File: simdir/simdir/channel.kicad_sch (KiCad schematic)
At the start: 84 parts, among them J1 Conn_Coaxial, Q1 BC847, Q10 BC847, Q11 BC847, Q12 BC847, Q13 BC847, Q14 BC847, Q15 BC847, Q16 BC847, Q2 BC847, Q3 BC847, Q4 BC847, Q5 BC847, Q6 BC847, Q7 BC847, Q8 BC847, Q9 BC847, U1 MASWSS0178, U10 MASWSS0178, U11 MASWSS0178, U12 MASWSS0178, U13 MASWSS0178, U14 MASWSS0178, U15 MASWSS0178, U16 MASWSS0178, U17 LTV-847S, U18 LTV-847S, U19 74HCT595, U2 MASWSS0178, U3 MASWSS0178, U4 MASWSS0178, U5 MASWSS0178, U6 MASWSS0178, U7 MASWSS0178, U8 MASWSS0178, U9 MASWSS0178

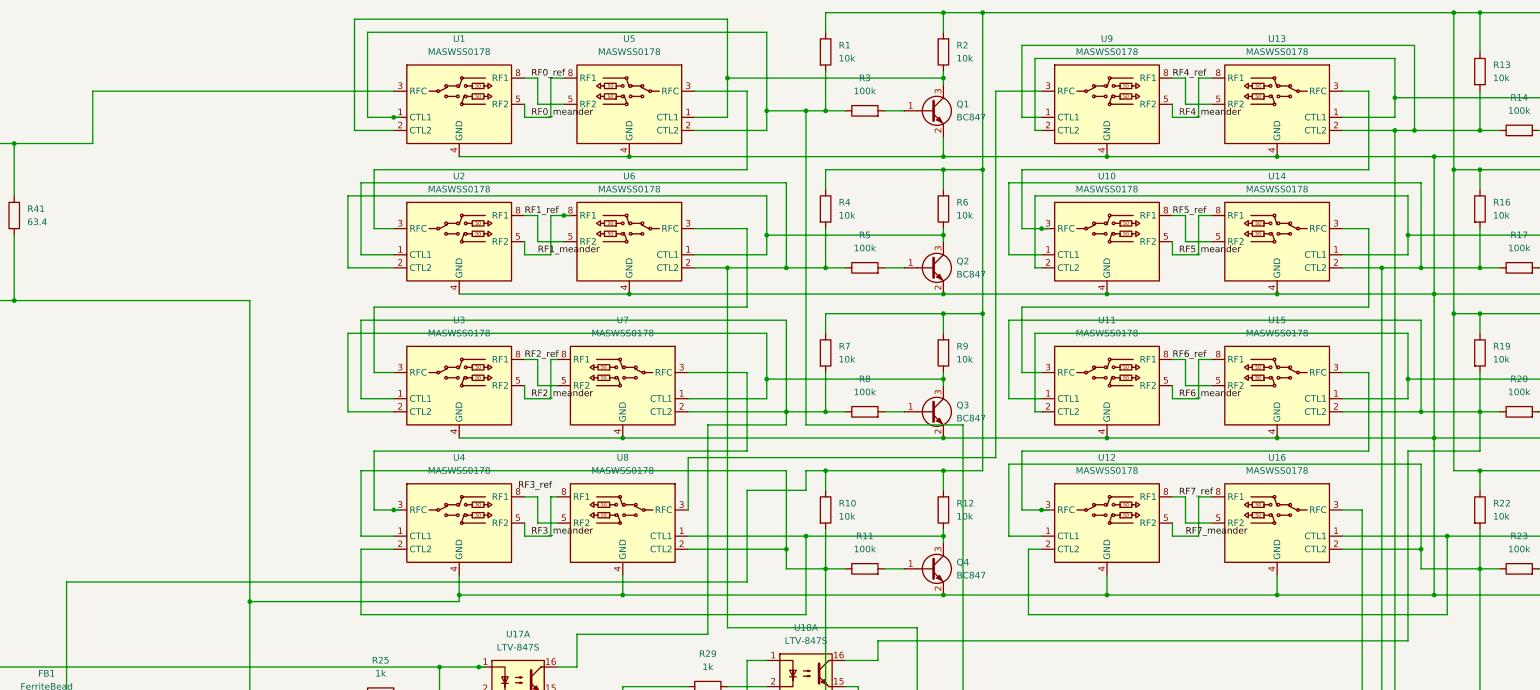
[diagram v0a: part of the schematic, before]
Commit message: Changed to new RF IC.
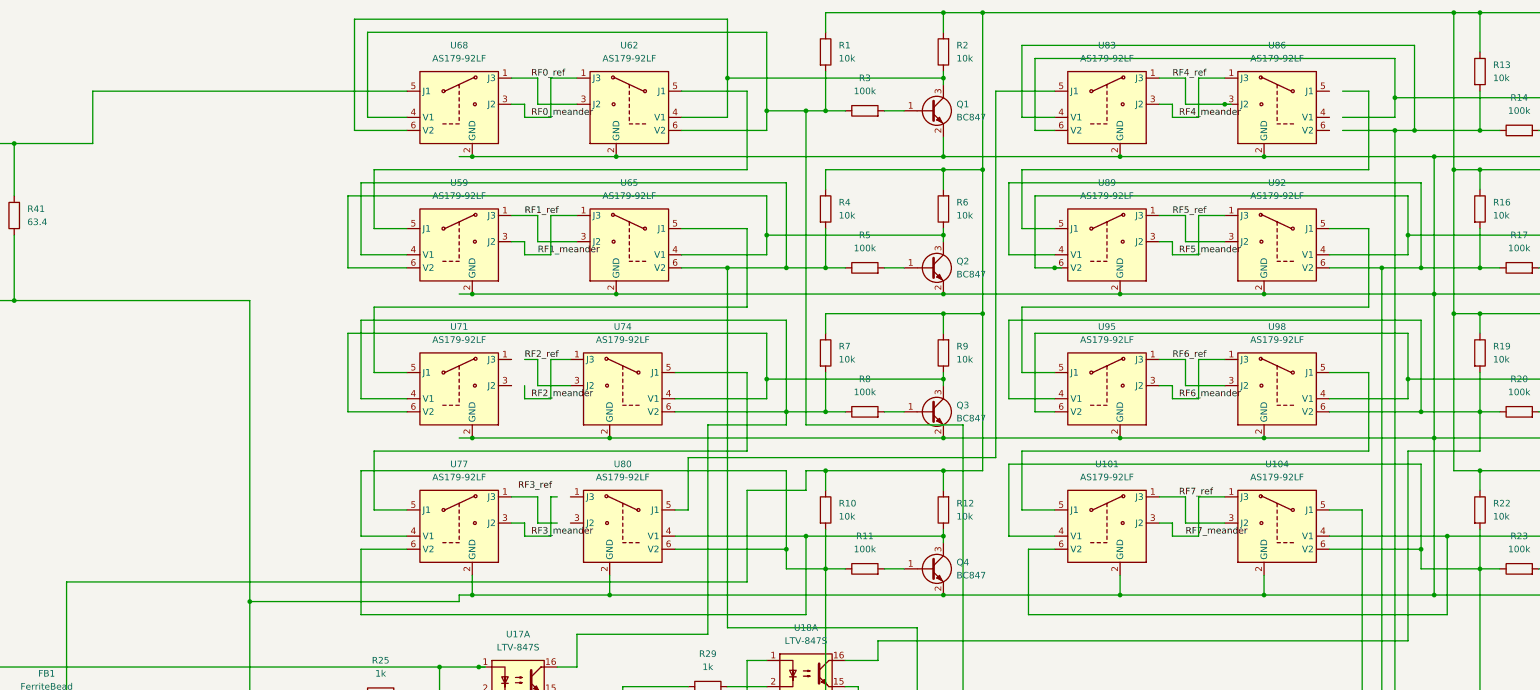
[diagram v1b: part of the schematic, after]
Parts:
- removed U1, U10, U11, U12, U13, U14, U15, U16, U2, U3, U4, U5, U6, U7, U8, U9: MASWSS0178, hand:MSOP-8-1EP_3x3mm_P0.65mm_EP1.73x1.85mm_hand, symbol hand:MASWSS0178
- added U101, U104, U59, U62, U65, U68, U71, U74, U77, U80, U83, U86, U89, U92, U95, U98: AS179-92LF, Package_TO_SOT_SMD:SOT-363_SC-70-6, symbol RF_Switch:AS179-92LF
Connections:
- net RF-In: now also U104.5 (J1)
- net RF0_meander: now also U62.1 (J3), U68.3 (J2)
- net RF0_ref: now also U62.3 (J2), U68.1 (J3)
- net RF1_meander: now also U59.3 (J2), U65.1 (J3)
- net RF1_ref: now also U59.1 (J3), U65.3 (J2)
- net RF2_meander: now also U74.1 (J3)
- net RF2_ref: now also U74.3 (J2)
- net RF3_meander: now also U77.3 (J2)
- net RF4_meander: now also U83.3 (J2), U86.1 (J3)
- net RF4_ref: now also U83.1 (J3), U86.3 (J2)
- net RF5_meander: now also U89.3 (J2), U92.1 (J3)
- net RF5_ref: now also U89.1 (J3), U92.3 (J2)
- net RF6_meander: now also U95.3 (J2), U98.1 (J3)
- net RF6_ref: now also U95.1 (J3), U98.3 (J2)
- net RF7_meander: now also U101.3 (J2), U104.1 (J3)
- net RF7_ref: now also U101.1 (J3), U104.3 (J2)
- net RF_GND: now also U101.2 (GND), U104.2 (GND), U59.2 (GND), U62.2 (GND), U65.2 (GND), U68.2 (GND), U71.2 (GND), U74.2 (GND), U77.2 (GND), U80.2 (GND), U83.2 (GND), U86.2 (GND), U89.2 (GND), U92.2 (GND), U95.2 (GND), U98.2 (GND)
- net at Q8.3 (C), R24.1: now also U101.6 (V2), U104.4 (V1)
- net at R1.2, R3.1, U18.10: now also U62.6 (V2), U68.4 (V1)
- net at R7.2, R8.1, U17.16: now also U71.4 (V1), U74.6 (V2)
- net at Q5.3 (C), R15.1: now also U83.6 (V2)
- net at R22.2, R23.1, U18.12: now also U101.4 (V1), U104.6 (V2)
- net at Q7.3 (C), R21.1: now also U95.6 (V2), U98.4 (V1)
- net at Q3.3 (C), R9.1: now also U71.6 (V2), U74.4 (V1)
- net at R4.2, R5.1, U18.14: now also U59.4 (V1), U65.6 (V2)
- net at Q2.3 (C), R6.1: now also U59.6 (V2), U65.4 (V1)
- net at Q6.3 (C), R18.1: now also U89.6 (V2), U92.4 (V1)
- net at R16.2, R17.1, U17.12: now also U89.4 (V1), U92.6 (V2)
- net at R10.2, R11.1, U17.14: now also U77.4 (V1), U80.6 (V2)
- net at Q1.3 (C), R2.1: now also U62.4 (V1), U68.6 (V2)
- net at Q4.3 (C), R12.1: now also U77.6 (V2), U80.4 (V1)
- net at R19.2, R20.1, U18.16: now also U95.4 (V1), U98.6 (V2)
- net at R41.2, R43.1: now also U68.5 (J1)
- net at R13.2, R14.1, U17.10: now also U83.4 (V1)
- new net: U65.5 (J1), U71.5 (J1)
- new net: U101.5 (J1), U98.5 (J1)
- new net: U59.5 (J1), U62.5 (J1)
- new net: U80.5 (J1), U83.5 (J1)
- new net: U92.5 (J1), U95.5 (J1)
- new net: U74.5 (J1), U77.5 (J1)

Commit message: Added decoupling capacitors between switch stages.
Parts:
- added C12, C15, C18, C21, C24, C27, C30, C33, C9: 100n, Capacitor_SMD:C_0805_2012Metric_Pad1.18x1.45mm_HandSolder, symbol Device:C
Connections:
- net RF-In: now also C33.2; no longer U104.5 (J1)
- net RF0_meander: now also U62.3 (J2), U68.1 (J3); no longer U62.1 (J3), U68.3 (J2)
- net RF0_ref: now also U62.1 (J3), U68.3 (J2); no longer U62.3 (J2), U68.1 (J3)
- net RF1_meander: now also U59.1 (J3), U65.3 (J2); no longer U59.3 (J2), U65.1 (J3)
- net RF1_ref: now also U59.3 (J2), U65.1 (J3); no longer U59.1 (J3), U65.3 (J2)
- net RF2_meander: now also U71.1 (J3), U74.3 (J2); no longer U74.1 (J3)
- net RF2_ref: now also U71.3 (J2), U74.1 (J3); no longer U74.3 (J2)
- net RF3_meander: now also U77.1 (J3), U80.3 (J2); no longer U77.3 (J2)
- net RF3_ref: now also U77.3 (J2), U80.1 (J3)
- net RF4_meander: now also U83.1 (J3), U86.3 (J2); no longer U83.3 (J2), U86.1 (J3)
- net RF4_ref: now also U83.3 (J2), U86.1 (J3); no longer U83.1 (J3), U86.3 (J2)
- net RF5_meander: now also U89.1 (J3), U92.3 (J2); no longer U89.3 (J2), U92.1 (J3)
- net RF5_ref: now also U89.3 (J2), U92.1 (J3); no longer U89.1 (J3), U92.3 (J2)
- net RF6_meander: now also U95.1 (J3), U98.3 (J2); no longer U95.3 (J2), U98.1 (J3)
- net RF6_ref: now also U95.3 (J2), U98.1 (J3); no longer U95.1 (J3), U98.3 (J2)
- net RF7_meander: now also U101.1 (J3), U104.3 (J2); no longer U101.3 (J2), U104.1 (J3)
- net RF7_ref: now also U101.3 (J2), U104.1 (J3); no longer U101.1 (J3), U104.3 (J2)
- net at Q8.3 (C), R24.1: now also U101.4 (V1), U104.6 (V2); no longer U101.6 (V2), U104.4 (V1)
- net at U59.6 (V2), U65.4 (V1): now also R4.2, R5.1, U18.14; no longer Q2.3 (C), R6.1
- net at U65.5 (J1): now also C15.1; no longer U71.5 (J1)
- net at R1.2, R3.1, U18.10: now also U62.4 (V1), U68.6 (V2); no longer U62.6 (V2), U68.4 (V1)
- net at R22.2, R23.1, U18.12: now also U101.6 (V2), U104.4 (V1); no longer U101.4 (V1), U104.6 (V2)
- net at U101.5 (J1): now also C30.2; no longer U98.5 (J1)
- net at R7.2, R8.1, U17.16: now also U71.6 (V2), U74.4 (V1); no longer U71.4 (V1), U74.6 (V2)
- net at Q5.3 (C), R15.1: now also U83.4 (V1), U86.6 (V2); no longer U83.6 (V2)
- net at Q1.3 (C), R2.1: now also U62.6 (V2), U68.4 (V1); no longer U62.4 (V1), U68.6 (V2)
- net at U62.5 (J1): now also C12.1; no longer U59.5 (J1)
- net at Q7.3 (C), R21.1: now also U95.4 (V1), U98.6 (V2); no longer U95.6 (V2), U98.4 (V1)
- net at Q3.3 (C), R9.1: now also U71.4 (V1), U74.6 (V2); no longer U71.6 (V2), U74.4 (V1)
- net at U86.4 (V1): now also R13.2, R14.1, U17.10, U83.6 (V2)
- net at U86.5 (J1): now also C24.1
- net at U77.6 (V2), U80.4 (V1): now also R10.2, R11.1, U17.14; no longer Q4.3 (C), R12.1
- net at U80.5 (J1): now also C21.1; no longer U83.5 (J1)
- net at Q6.3 (C), R18.1: now also U89.4 (V1), U92.6 (V2); no longer U89.6 (V2), U92.4 (V1)
- net at R19.2, R20.1, U18.16: now also U95.6 (V2), U98.4 (V1); no longer U95.4 (V1), U98.6 (V2)
- net at R41.2, R43.1: now also C9.1; no longer U68.5 (J1)
- net at U92.5 (J1): now also C27.1; no longer U95.5 (J1)
- net at R16.2, R17.1, U17.12: now also U89.6 (V2), U92.4 (V1); no longer U89.4 (V1), U92.6 (V2)
- net at U74.5 (J1): now also C18.1; no longer U77.5 (J1)
- net at U89.5 (J1): now also C24.2
- new net: Q2.3 (C), R6.1, U59.4 (V1), U65.6 (V2)
- new net: C33.1, U104.5 (J1)
- new net: C12.2, U59.5 (J1)
- new net: Q4.3 (C), R12.1, U77.4 (V1), U80.6 (V2)
- new net: C9.2, U68.5 (J1)
- new net: C15.2, U71.5 (J1)
- new net: C30.1, U98.5 (J1)
- new net: C18.2, U77.5 (J1)
- new net: C21.2, U83.5 (J1)
- new net: C27.2, U95.5 (J1)
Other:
- moved on the sheet: Q5, Q6, Q7, Q8, R13, R14, R15, R16, R17, R18, R19, R20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

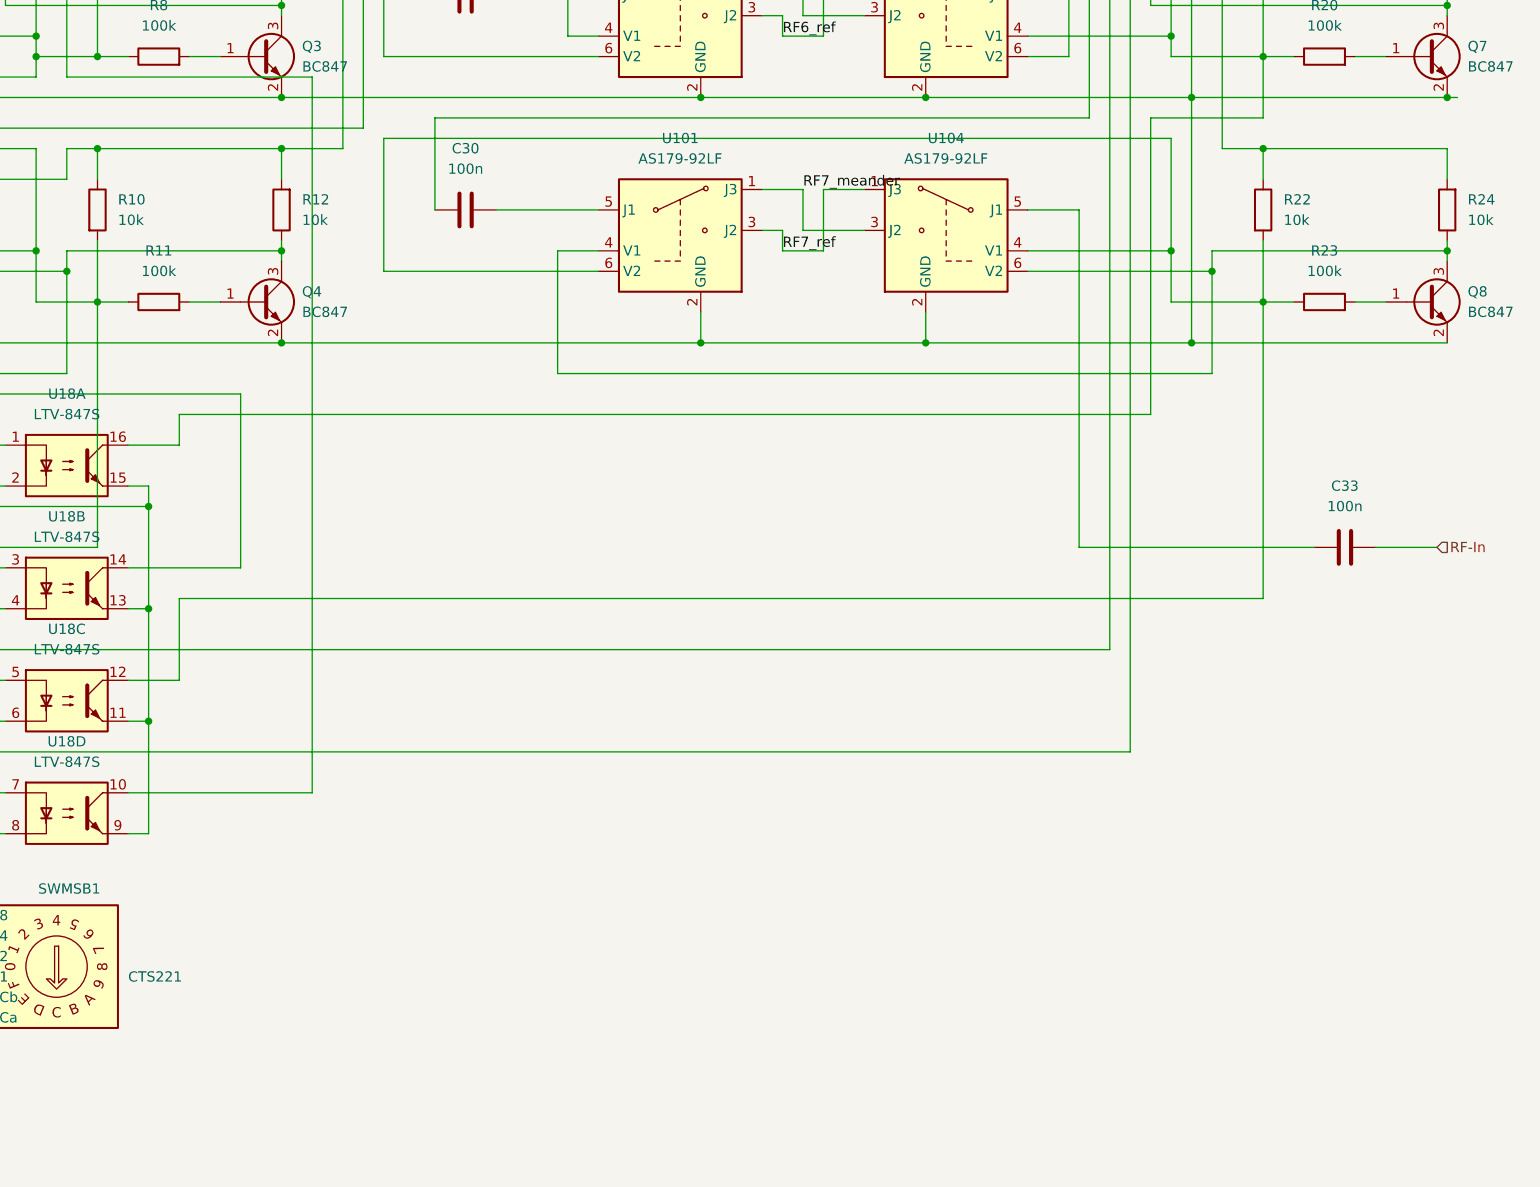
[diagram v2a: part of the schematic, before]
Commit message: Fixed routing for N.
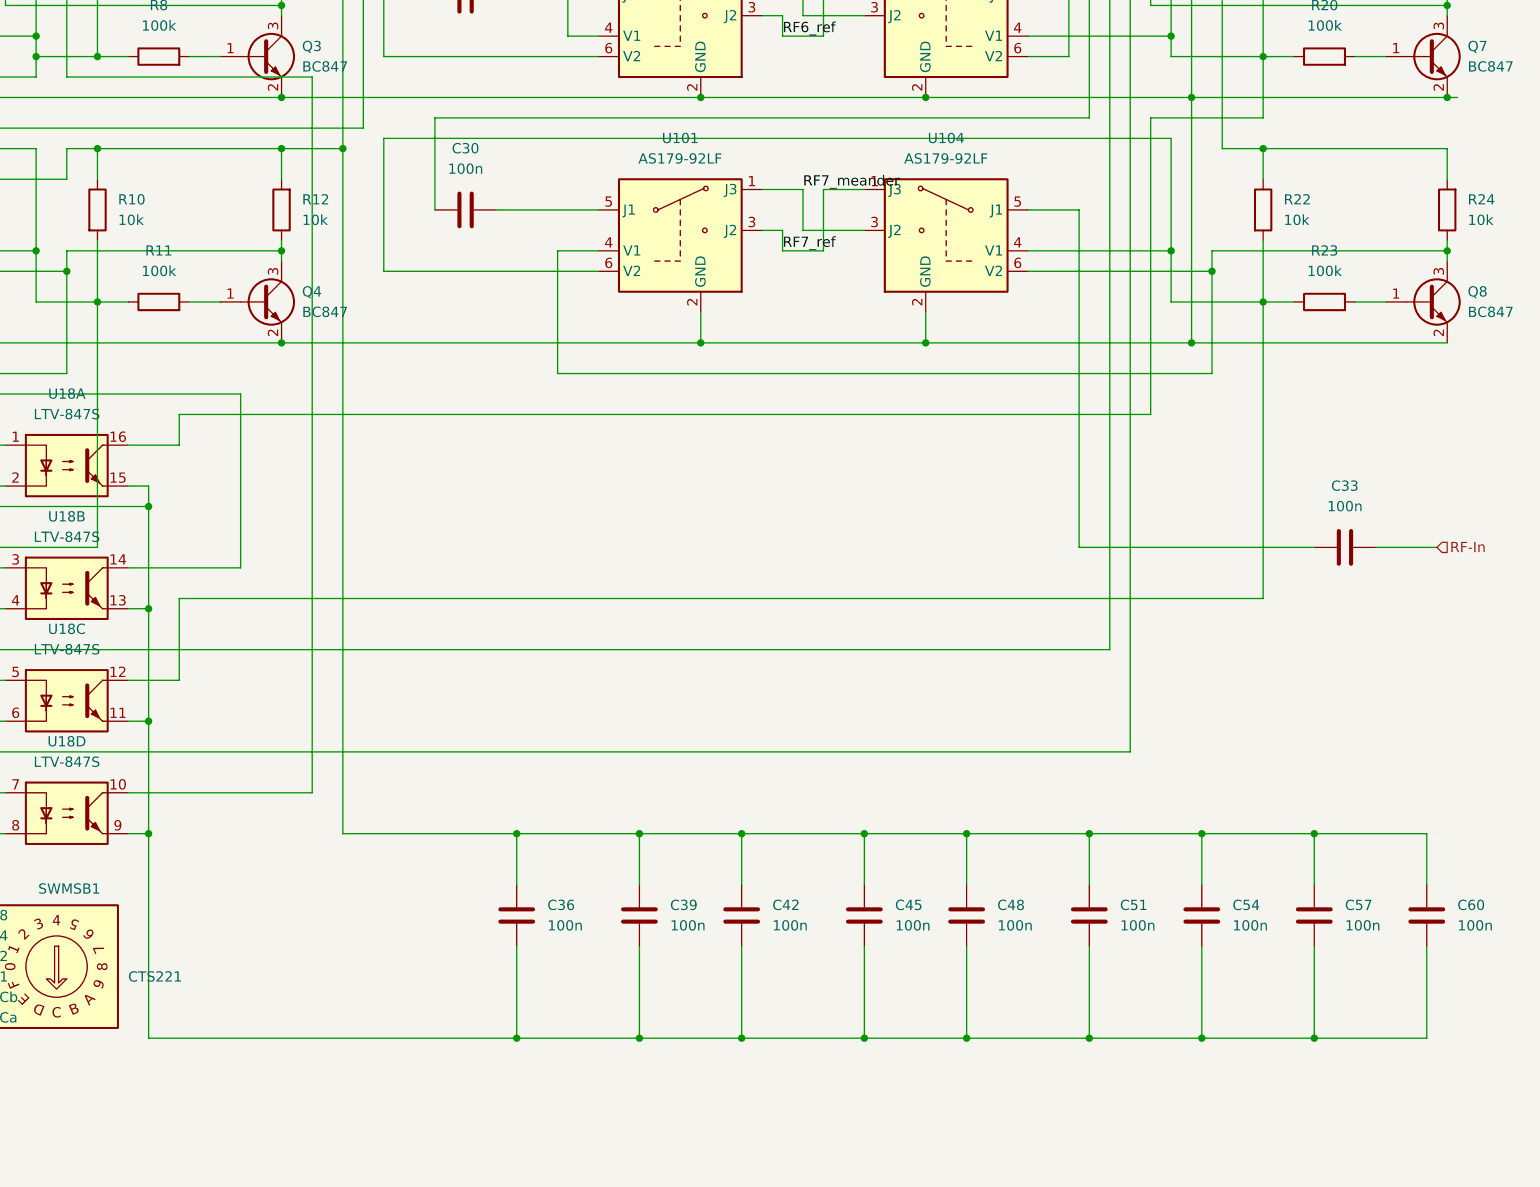
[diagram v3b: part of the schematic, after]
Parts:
- added C36, C39, C42, C45, C48, C51, C54, C57, C60: 100n, Capacitor_SMD:C_0805_2012Metric_Pad1.18x1.45mm_HandSolder, symbol Device:C
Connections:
- net RF_GND: now also C36.2, C39.2, C42.2, C45.2, C48.2, C51.2, C54.2, C57.2, C60.2
- net at C1.1, FB1.2, R1.1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: now also C36.1, C39.1, C42.1, C45.1, C48.1, C51.1, C54.1, C57.1, C60.1

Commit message: Changed to 8-pin connector + added more ground planes.
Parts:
- C12, C15, C18, C21, C24, C27, C30, C33, C9: value 100n -> 10n
- R1, R10, R12, R13, R15, R16, R18, R19, R2, R21, R22, R24, R4, R6, R7, R9: value 10k -> 1.5k
- R11, R14, R17, R20, R23, R3, R5, R8: value 100k -> 47k
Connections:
- net RF-5v: now reaches C1.1, C36.1, C39.1, C42.1, C45.1, C48.1, C51.1, C54.1, C57.1, C60.1, FB1.2, R1.1, R10.1, R12.2, R13.1, R15.2, R16.1, R18.2, R19.1, R2.2, R21.2, R22.1, R24.2, R4.1, R6.2, R7.1, R9.2
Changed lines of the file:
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@@
 		)
 	)
+	(label "RF-5v"
+		(at 62.23 132.08 0)
+		(effects
+			(font
+				(size 1.27 1.27)
+			)
+			(justify left bottom)
+		)
+	)
 	(label "RF5_meander"
 		(at 297.18 60.96 0)
@@
 			)
 		)
-		(property "Value" "10k"
+		(property "Value" "1.5k"
 			(at 379.73 119.3799 0)
 			(show_name no)
@@
 			)
 		)
-		(property "Value" "100k"
+		(property "Value" "47k"
 			(at 217.17 36.83 90)
 			(show_name no)
@@
 			)
 		)
-		(property "Value" "10k"
+		(property "Value" "1.5k"
 			(at 212.09 30.4799 0)
 			(show_name no)
@@
 			)
 		)
-		(property "Value" "100n"
+		(property "Value" "10n"
 			(at 364.49 154.94 90)
 			(show_name no)
@@
 			)
 		)
-		(property "Value" "10k"
+		(property "Value" "1.5k"
 			(at 356.87 119.3799 0)
 			(show_name no)
@@
 			)
 		)
-		(property "Value" "100n"
+		(property "Value" "10n"
 			(at 109.22 58.42 90)
 			(show_name no)
@@
 			)
 		)
-		(property "Value" "10k"
+		(property "Value" "1.5k"
 			(at 379.73 88.8999 0)
 			(show_name no)
@@
 			)
 		)
-		(property "Value" "10k"
+		(property "Value" "1.5k"
 			(at 212.09 60.9599 0)
 			(show_name no)
@@
 			)
 		)
-		(property "Value" "10k"
+		(property "Value" "1.5k"
 			(at 234.95 30.4799 0)
 			(show_name no)
@@
 			)
 		)
-		(property "Value" "100n"
+		(property "Value" "10n"
 			(at 85.09 31.75 90)
 			(show_name no)
@@
 			)
 		)
-		(property "Value" "100n"
+		(property "Value" "10n"
 			(at 110.49 86.36 90)
 			(show_name no)
@@
 			)
 		)
-		(property "Value" "100k"
+		(property "Value" "47k"
 			(at 361.95 95.25 90)
 			(show_name no)
@@
 			)
 		)
-		(property "Value" "100k"
+		(property "Value" "47k"
 			(at 217.17 125.73 90)
 			(show_name no)
@@
 			)
 		)
-		(property "Value" "100k"
+		(property "Value" "47k"
 			(at 217.17 95.25 90)
 			(show_name no)
@@
 			)
 		)
-		(property "Value" "100k"
+		(property "Value" "47k"
 			(at 361.95 40.64 90)
 			(show_name no)
@@
 			)
 		)
-		(property "Value" "10k"
+		(property "Value" "1.5k"
 			(at 234.95 119.3799 0)
 			(show_name no)
@@
 			)
 		)
-		(property "Value" "10k"
+		(property "Value" "1.5k"
 			(at 234.95 60.9599 0)
 			(show_name no)
@@
 			)
 		)
-		(property "Value" "10k"
+		(property "Value" "1.5k"
 			(at 356.87 88.8999 0)
 			(show_name no)
@@
 			)
 		)
-		(property "Value" "100n"
+		(property "Value" "10n"
 			(at 110.49 113.03 90)
 			(show_name no)
@@
 			)
 		)
-		(property "Value" "10k"
+		(property "Value" "1.5k"
 			(at 212.09 88.8999 0)
 			(show_name no)
@@
 			)
 		)
-		(property "Value" "100k"
+		(property "Value" "47k"
 			(at 361.95 125.73 90)
 			(show_name no)
@@
 			)
 		)
-		(property "Value" "10k"
+		(property "Value" "1.5k"
 			(at 379.73 60.9599 0)
 			(show_name no)
@@
 			)
 		)
-		(property "Value" "10k"
+		(property "Value" "1.5k"
 			(at 212.09 119.3799 0)
 			(show_name no)
@@
 			)
 		)
-		(property "Value" "100k"
+		(property "Value" "47k"
 			(at 217.17 67.31 90)
 			(show_name no)
@@
 			)
 		)
-		(property "Value" "10k"
+		(property "Value" "1.5k"
 			(at 379.73 34.2899 0)
 			(show_name no)
@@
 			)
 		)
-		(property "Value" "10k"
+		(property "Value" "1.5k"
 			(at 234.95 88.8999 0)
 			(show_name no)
@@
 			)
 		)
-		(property "Value" "100n"
+		(property "Value" "10n"
 			(at 255.27 31.75 90)
 			(show_name no)
@@
 			)
 		)
-		(property "Value" "100k"
+		(property "Value" "47k"
 			(at 361.95 67.31 90)
 			(show_name no)
@@
 			)
 		)
-		(property "Value" "10k"
+		(property "Value" "1.5k"
 			(at 356.87 34.2899 0)
 			(show_name no)
@@
 			)
 		)
-		(property "Value" "100n"
+		(property "Value" "10n"
 			(at 255.27 86.36 90)
 			(show_name no)
@@
 			)
 		)
-		(property "Value" "100n"
+		(property "Value" "10n"
 			(at 255.27 113.03 90)
 			(show_name no)
@@
 			)
 		)
-		(property "Value" "10k"
+		(property "Value" "1.5k"
 			(at 356.87 60.9599 0)
 			(show_name no)
@@
 			)
 		)
-		(property "Value" "100n"
+		(property "Value" "10n"
 			(at 255.27 58.42 90)
 			(show_name no)
